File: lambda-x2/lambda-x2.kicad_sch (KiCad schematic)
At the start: 109 parts, among them J1 FTSH-107-01-F-DV-K, J2 Conn_02x06_Top_Bottom, J3 Conn_02x02_Odd_Even, J4 Conn_01x10, Q2 BTS3028, U1 MCP6004, U2 STM32F103C6Tx, U3 GS8332, U4 LM78M05_TO252, U5 XC6206P332MR, U6 REF3033, U7 MCP6002T-I/SN, U8 TJA1051T-3

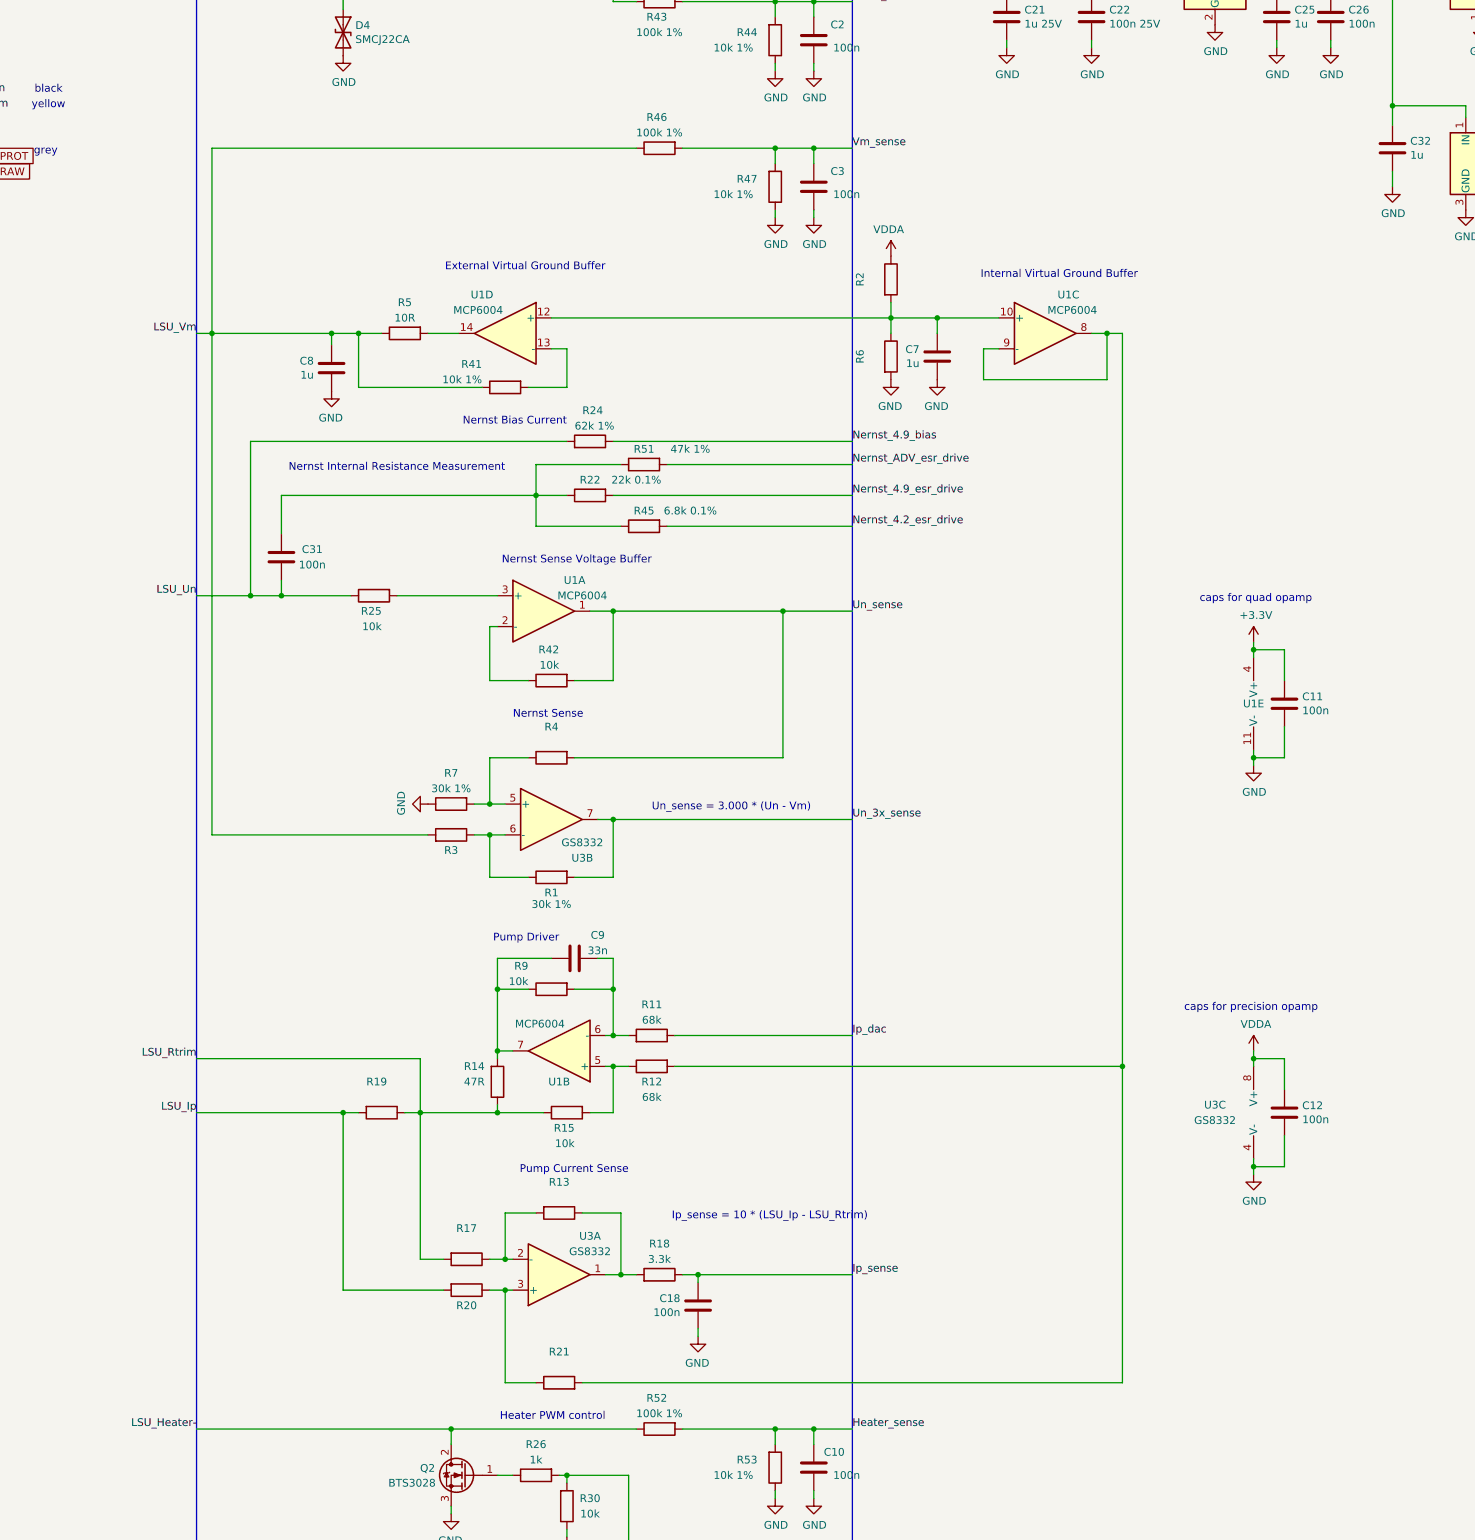
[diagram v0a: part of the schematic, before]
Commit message: lambda-x2: move analog frontend to separate sheet
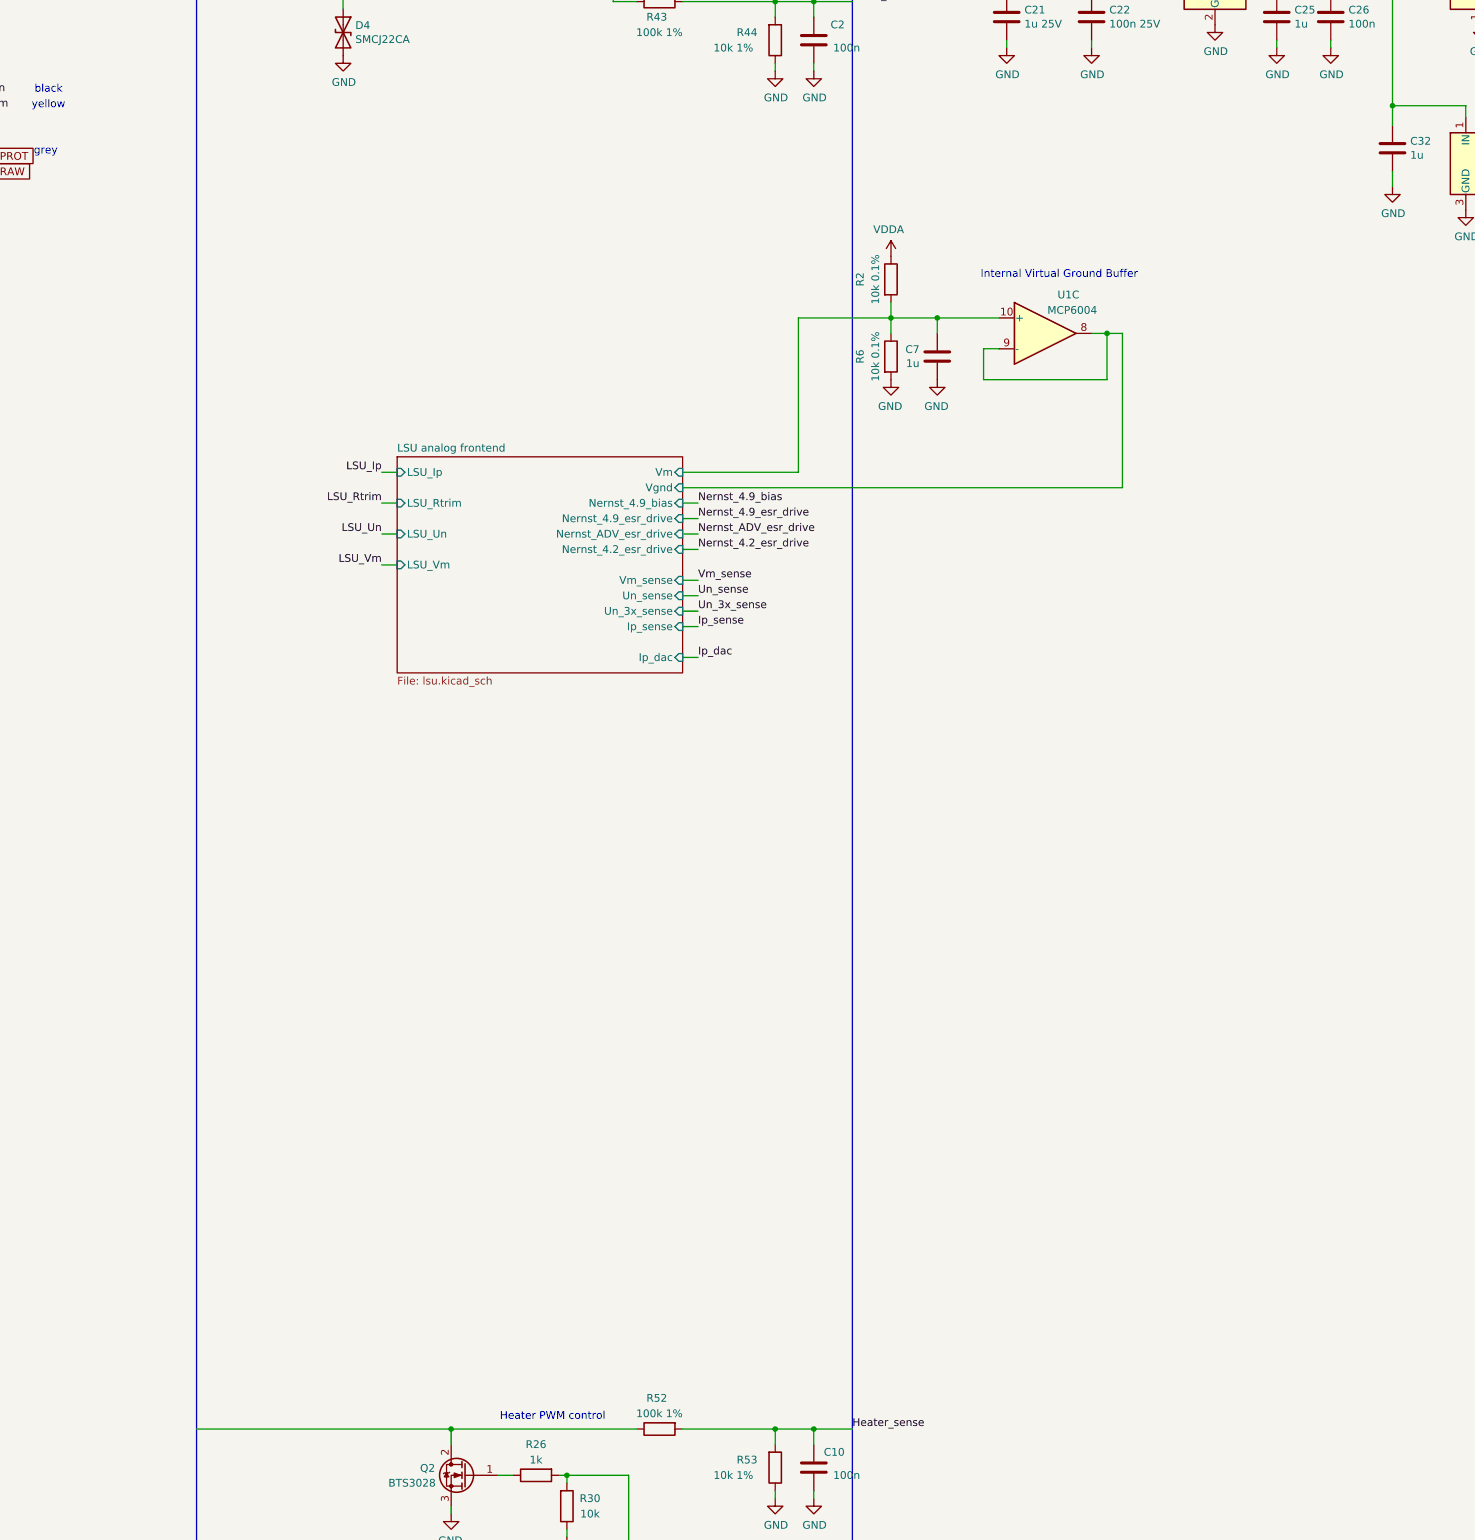
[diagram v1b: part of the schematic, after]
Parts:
- removed C11, C12, C18, C3, C31: 100n, Capacitor_SMD:C_0402_1005Metric, symbol Device:C
- removed C8: 1u, Capacitor_SMD:C_0402_1005Metric, symbol Device:C
- removed C9: 33n, Capacitor_SMD:C_0402_1005Metric, symbol Device:C
- removed R1, R7: 30k 1%, Resistor_SMD:R_0603_1608Metric, symbol Device:R
- removed R11, R12: 68k, Resistor_SMD:R_0402_1005Metric, symbol Device:R
- removed R13, R17, R19, R20, R21, R3, R4: (no value), symbol Device:R
- removed R14: 47R, Resistor_SMD:R_0603_1608Metric, symbol Device:R
- removed R15, R25, R42, R9: 10k, Resistor_SMD:R_0402_1005Metric, symbol Device:R
- removed R18: 3.3k, Resistor_SMD:R_0402_1005Metric, symbol Device:R
- removed R22: 22k 0.1%, Resistor_SMD:R_0603_1608Metric, symbol Device:R
- removed R24: 62k 1%, Resistor_SMD:R_0603_1608Metric, symbol Device:R
- removed R41, R47: 10k 1%, Resistor_SMD:R_0402_1005Metric, symbol Device:R
- removed R45: 6.8k 0.1%, Resistor_SMD:R_0603_1608Metric, symbol Device:R
- removed R46: 100k 1%, Resistor_SMD:R_0402_1005Metric, symbol Device:R
- removed R5: 10R, Resistor_SMD:R_1206_3216Metric, symbol Device:R
- removed R51: 47k 1%, Resistor_SMD:R_0603_1608Metric, symbol Device:R
- removed unit 1 of U1
- removed unit 4 of U1
- removed unit 5 of U1
- removed unit 2 of U1
- removed U3: GS8332, Package_SO:TSSOP-8_3x3mm_P0.65mm, symbol Amplifier_Operational:TL072
- R2, R6: value (none) -> 10k 0.1%; footprint (none) -> Resistor_SMD:R_0603_1608Metric
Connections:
- net LSU_Heater-: no longer Q2.2 (D), R52.1
- net LSU analog frontend/Vm: now reaches C7.1, R2.2, R6.1, U1.10 (+)
- net LSU analog frontend/Vgnd: now reaches U1.8, U1.9 (-)
- new net: Q2.2 (D), R52.1
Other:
- added sheet LSU analog frontend (lsu.kicad_sch)
- note removed: "External Virtual Ground Buffer"
- note removed: "Ip_sense = 10 * (LSU_Ip - LSU_Rtrim)"
- note removed: "Nernst Bias Current"
- note removed: "Nernst Internal Resistance Measurement"
- note removed: "Nernst Sense"
- note removed: "Nernst Sense Voltage Buffer"
- note removed: "Pump Current Sense"
- note removed: "Pump Driver"
- note removed: "Un_sense = 3.000 * (Un - Vm)"
- note removed: "caps for precision opamp"
- note removed: "caps for quad opamp"

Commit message: Progress
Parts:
- removed J2: Conn_02x06_Top_Bottom, db_footprints:MX120G_12, symbol Connector_Generic:Conn_02x06_Top_Bottom
- removed U1: MCP6004, Package_SO:TSSOP-14_4.4x5mm_P0.65mm, symbol Amplifier_Operational:MCP6004
- added P1: 33311-24AW-2, local:33311-24AW-2, symbol 33311-24AW-2:33311-24AW-2
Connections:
- net 12V_RAW: now also P1.2 (A2)
- net CAN_H: now also P1.21 (C5)
- net CAN_L: now also P1.22 (C6)
- net GND: now also P1.1 (A1)
- net L_LSU_Heater-: now reaches Q2.2 (D), R52.1
- net L_LSU_Heater-: now also P1.17 (C1)
- net Heater_sense renamed l_Heater_sense
- net l_Heater_sense: no longer U2.19 (PB1)
- net Ip_dac renamed L_Ip_dac
- net Ip_sense renamed L_Ip_sense
- net LSU analog left/Vm renamed LSU analog left/Vgnd_ref
- net Un_3x_sense renamed L_Un_3x_sense
- net Un_sense renamed L_Un_sense
- net Vm_sense renamed L_Vm_sense
- net heater_pwm renamed L_heater_pwm
- new net L_Heater_sense: U2.19 (PB1)
- new net L_LSU_Ip: P1.18 (C2)
- new net L_LSU_Rtrim: P1.11 (B3)
- new net L_LSU_Un: P1.19 (C3)
- new net L_LSU_Vm: P1.10 (B2)
- new net R_LSU_Heater-: P1.8 (A8)
- new net R_LSU_Ip: P1.7 (A7)
- new net R_LSU_Rtrim: P1.14 (B6)
- new net R_LSU_Un: P1.6 (A6)
- new net R_LSU_Vm: P1.15 (B7)
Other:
- sheet LSU analog frontend renamed LSU analog left
- added sheet LSU analog right (lsu.kicad_sch)
- sheet LSU analog left ports: added Vgnd_ref; removed Vgnd, Vm
- note removed: "Internal Virtual Ground Buffer"
- note removed: "MX120G External I/O connector (or use through holes for integration)"
- moved on the sheet: C7, R2, R6

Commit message: progress
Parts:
- J3: value Conn_02x02_Odd_Even -> (none); footprint Connector_PinHeader_2.54mm:PinHeader_2x02_P2.54mm_Vertical -> (none); now left out of the parts list
- J4: value Conn_01x10 -> (none); footprint Connector_PinHeader_2.54mm:PinHeader_1x10_P2.54mm_Vertical -> (none); now left out of the parts list
- TP1, TP2: value TestPoint -> (none); footprint Connector_PinHeader_2.54mm:PinHeader_1x01_P2.54mm_Vertical -> (none); now left out of the parts list
- TP3, TP4, TP5: value TestPoint -> (none); footprint TestPoint:TestPoint_Pad_D1.0mm -> (none); now left out of the parts list
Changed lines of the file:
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@@
   )
   (symbol (lib_id "Connector_Generic:Conn_02x02_Odd_Even") (at 551.815 62.865 0) (unit 1)
-    (in_bom yes) (on_board yes)
+    (in_bom no) (on_board yes)
     (property "Reference" "J3" (id 0) (at 553.085 57.3532 0))
-    (property "Value" "Conn_02x02_Odd_Even" (id 1) (at 553.085 59.6646 0))
-    (property "Footprint" "Connector_PinHeader_2.54mm:PinHeader_2x02_P2.54mm_Vertical" (id 2) (at 551.815 62.865 0)
+    (property "Value" "" (id 1) (at 553.085 59.6646 0))
+    (property "Footprint" "" (id 2) (at 551.815 62.865 0)
       (effects (font (size 1.27 1.27)) hide)
     )
@@
   )
   (symbol (lib_id "Connector:TestPoint") (at 385.445 283.21 90) (unit 1)
-    (in_bom yes) (on_board yes)
+    (in_bom no) (on_board yes)
     (property "Reference" "TP1" (id 0) (at 383.6162 278.257 90))
-    (property "Value" "TestPoint" (id 1) (at 383.6162 280.5684 90))
-    (property "Footprint" "Connector_PinHeader_2.54mm:PinHeader_1x01_P2.54mm_Vertical" (id 2) (at 385.445 278.13 0)
+    (property "Value" "" (id 1) (at 383.6162 280.5684 90))
+    (property "Footprint" "" (id 2) (at 385.445 278.13 0)
       (effects (font (size 1.27 1.27)) hide)
     )
@@
   )
   (symbol (lib_id "Connector:TestPoint") (at 374.015 291.465 180) (unit 1)
-    (in_bom yes) (on_board yes)
+    (in_bom no) (on_board yes)
     (property "Reference" "TP2" (id 0) (at 375.4882 292.1254 0)
       (effects (font (size 1.27 1.27)) (justify right))
     )
-    (property "Value" "TestPoint" (id 1) (at 375.4882 294.4368 0)
+    (property "Value" "" (id 1) (at 375.4882 294.4368 0)
       (effects (font (size 1.27 1.27)) (justify right))
     )
-    (property "Footprint" "Connector_PinHeader_2.54mm:PinHeader_1x01_P2.54mm_Vertical" (id 2) (at 368.935 291.465 0)
+    (property "Footprint" "" (id 2) (at 368.935 291.465 0)
       (effects (font (size 1.27 1.27)) hide)
     )
@@
   )
   (symbol (lib_id "Connector_Generic:Conn_01x10") (at 478.79 303.53 0) (unit 1)
-    (in_bom yes) (on_board yes)
+    (in_bom no) (on_board yes)
     (property "Reference" "J4" (id 0) (at 480.822 303.7332 0)
       (effects (font (size 1.27 1.27)) (justify left))
     )
-    (property "Value" "Conn_01x10" (id 1) (at 480.822 306.0446 0)
-      (effects (font (size 1.27 1.27)) (justify left))
-    )
-    (property "Footprint" "Connector_PinHeader_2.54mm:PinHeader_1x10_P2.54mm_Vertical" (id 2) (at 478.79 303.53 0)
+    (property "Value" "" (id 1) (at 480.822 306.0446 0)
+      (effects (font (size 1.27 1.27)) (justify left))
+    )
+    (property "Footprint" "" (id 2) (at 478.79 303.53 0)
       (effects (font (size 1.27 1.27)) hide)
     )
@@
   )
   (symbol (lib_id "Connector:TestPoint") (at 440.69 321.31 270) (unit 1)
-    (in_bom yes) (on_board yes)
+    (in_bom no) (on_board yes)
     (property "Reference" "TP4" (id 0) (at 445.77 321.31 90)
       (effects (font (size 1.27 1.27)) (justify left))
     )
-    (property "Value" "TestPoint" (id 1) (at 445.77 322.5799 90)
+    (property "Value" "" (id 1) (at 445.77 322.5799 90)
       (effects (font (size 1.27 1.27)) (justify left) hide)
     )
-    (property "Footprint" "TestPoint:TestPoint_Pad_D1.0mm" (id 2) (at 440.69 326.39 0)
+    (property "Footprint" "" (id 2) (at 440.69 326.39 0)
       (effects (font (size 1.27 1.27)) hide)
     )
@@
   )
   (symbol (lib_id "Connector:TestPoint") (at 440.69 316.23 270) (unit 1)
-    (in_bom yes) (on_board yes)
+    (in_bom no) (on_board yes)
     (property "Reference" "TP5" (id 0) (at 445.77 316.23 90)
       (effects (font (size 1.27 1.27)) (justify left))
     )
-    (property "Value" "TestPoint" (id 1) (at 445.77 317.4999 90)
+    (property "Value" "" (id 1) (at 445.77 317.4999 90)
       (effects (font (size 1.27 1.27)) (justify left) hide)
     )
-    (property "Footprint" "TestPoint:TestPoint_Pad_D1.0mm" (id 2) (at 440.69 321.31 0)
+    (property "Footprint" "" (id 2) (at 440.69 321.31 0)
       (effects (font (size 1.27 1.27)) hide)
     )
@@
   )
   (symbol (lib_id "Connector:TestPoint") (at 440.69 318.77 270) (unit 1)
-    (in_bom yes) (on_board yes)
+    (in_bom no) (on_board yes)
     (property "Reference" "TP3" (id 0) (at 445.77 318.77 90)
       (effects (font (size 1.27 1.27)) (justify left))
     )
-    (property "Value" "TestPoint" (id 1) (at 445.77 320.0399 90)
+    (property "Value" "" (id 1) (at 445.77 320.0399 90)
       (effects (font (size 1.27 1.27)) (justify left) hide)
     )
-    (property "Footprint" "TestPoint:TestPoint_Pad_D1.0mm" (id 2) (at 440.69 323.85 0)
-      (effects (font (size 1.27 1.27)) hide)
-    )
+    (property "Footprint" "" (id 2) (at 440.69 323.85 0)
+      (effects (font (size 1.27 1.27)) hide)
+    )

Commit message: Update components
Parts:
- D6: LCSC C2128 -> C81598
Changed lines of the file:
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@@
       (effects (font (size 1.27 1.27)) hide)
     )
-    (property "LCSC" "C2128" (id 4) (at 227.33 34.29 0)
+    (property "LCSC" "C81598" (id 4) (at 227.33 34.29 0)
       (effects (font (size 1.27 1.27)) hide)
     )
